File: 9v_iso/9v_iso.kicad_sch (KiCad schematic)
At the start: 15 parts, among them J1 Conn_01x02, J2 Conn_01x02, J3 Conn_01x03, U1 ICZ_SINGLE

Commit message: Checkpoint.
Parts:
- removed JP1: SolderJumper_3_Open, Jumper:SolderJumper-3_P1.3mm_Open_RoundedPad1.0x1.5mm_NumberLabels, symbol Jumper:SolderJumper_3_Open
- J3: value Conn_01x03 -> DNI
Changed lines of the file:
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@@
   (junction (at 59.69 73.66) (diameter 0) (color 0 0 0 0)
   )
-  (junction (at 99.06 49.53) (diameter 0) (color 0 0 0 0)
-  )
   (junction (at 99.06 64.77) (diameter 0) (color 0 0 0 0)
   )
-  (junction (at 93.98 46.99) (diameter 0) (color 0 0 0 0)
-  )
   (junction (at 50.8 90.17) (diameter 0) (color 0 0 0 0)
   )
@@
   (junction (at 59.69 90.17) (diameter 0) (color 0 0 0 0)
   )
-  (junction (at 88.9 44.45) (diameter 0) (color 0 0 0 0)
-  )
   (junction (at 78.74 90.17) (diameter 0) (color 0 0 0 0)
   )
@@
     (stroke (width 0) (type default) (color 0 0 0 0))
   )
-  (wire (pts (xy 88.9 39.37) (xy 88.9 44.45))
-    (stroke (width 0) (type default) (color 0 0 0 0))
-  )
   (wire (pts (xy 125.73 90.17) (xy 132.08 90.17))
     (stroke (width 0) (type default) (color 0 0 0 0))
@@
     (stroke (width 0) (type default) (color 0 0 0 0))
   )
-  (wire (pts (xy 93.98 43.18) (xy 93.98 46.99))
-    (stroke (width 0) (type default) (color 0 0 0 0))
-  )
   (wire (pts (xy 132.08 90.17) (xy 135.89 90.17))
     (stroke (width 0) (type default) (color 0 0 0 0))
@@
   )
   (wire (pts (xy 241.3 86.36) (xy 241.3 93.98))
-    (stroke (width 0) (type default) (color 0 0 0 0))
-  )
-  (wire (pts (xy 99.06 39.37) (xy 99.06 49.53))
     (stroke (width 0) (type default) (color 0 0 0 0))
   )
@@
       (effects (font (size 1.27 1.27)) (justify left))
     )
-    (property "Value" "Conn_01x03" (id 1) (at 111.76 48.2599 0)
+    (property "Value" "DNI" (id 1) (at 111.76 48.2599 0)
       (effects (font (size 1.27 1.27)) (justify left))
     )
@@
     (pin "2")
   )
-  (symbol (lib_id "Jumper:SolderJumper_3_Open") (at 93.98 39.37 0) (unit 1)
-    (in_bom yes) (on_board yes) (fields_autoplaced)
-    (property "Reference" "JP1" (id 0) (at 93.98 33.02 0))
-    (property "Value" "SolderJumper_3_Open" (id 1) (at 93.98 35.56 0))
-    (property "Footprint" "Jumper:SolderJumper-3_P1.3mm_Open_RoundedPad1.0x1.5mm_NumberLabels" (id 2) (at 93.98 39.37 0)
-      (effects (font (size 1.27 1.27)) hide)
-    )
-    (property "Datasheet" "~" (id 3) (at 93.98 39.37 0)
-      (effects (font (size 1.27 1.27)) hide)
-    )
-    (pin "1")
-    (pin "2")
-    (pin "3")
-  )
   (symbol (lib_id "power:GND") (at 88.9 46.99 0) (unit 1)
     (in_bom yes) (on_board yes) (fields_autoplaced)
@@
     )
     (path "/046a65e2-4a4e-47f4-924b-a6c9951d2ed3"
-      (reference "J3") (unit 1) (value "Conn_01x03") (footprint "Connector_PinHeader_2.54mm:PinHeader_1x03_P2.54mm_Vertical")
-    )
-    (path "/cbd2c5b4-c432-4ac8-b664-5d523c14cd16"
-      (reference "JP1") (unit 1) (value "SolderJumper_3_Open") (footprint "Jumper:SolderJumper-3_P1.3mm_Open_RoundedPad1.0x1.5mm_NumberLabels")
+      (reference "J3") (unit 1) (value "DNI") (footprint "Connector_PinHeader_2.54mm:PinHeader_1x03_P2.54mm_Vertical")
     )
     (path "/91a6582d-c885-450f-87a6-af7126326a3e"

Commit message: checkpoint
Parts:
- added R1: DNI/0, Resistor_SMD:R_0805_2012Metric_Pad1.20x1.40mm_HandSolder, symbol Device:R
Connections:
- net at J3.2 (Pin_2): now also R1.1; no longer U1.3 (ON/~{OFF})
- new net: R1.2, U1.3 (ON/~{OFF})
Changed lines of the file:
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@@
+    (stroke (width 0) (type default) (color 0 0 0 0))
+  )
+  (wire (pts (xy 93.98 46.99) (xy 93.98 54.61))
+    (stroke (width 0) (type default) (color 0 0 0 0))
+  )
+  (wire (pts (xy 93.98 62.23) (xy 93.98 85.09))
     (stroke (width 0) (type default) (color 0 0 0 0))
   )
@@
   )
   (wire (pts (xy 106.68 104.14) (xy 99.06 104.14))
-    (stroke (width 0) (type default) (color 0 0 0 0))
-  )
-  (wire (pts (xy 93.98 46.99) (xy 93.98 85.09))
     (stroke (width 0) (type default) (color 0 0 0 0))
   )
@@
     )
     (property "Datasheet" "~" (id 3) (at 59.69 82.55 0)
+      (effects (font (size 1.27 1.27)) hide)
+    )
+    (pin "1")
+    (pin "2")
+  )
+  (symbol (lib_id "Device:R") (at 93.98 58.42 0) (unit 1)
+    (in_bom yes) (on_board yes) (fields_autoplaced)
+    (property "Reference" "R1" (id 0) (at 96.52 57.1499 0)
+      (effects (font (size 1.27 1.27)) (justify left))
+    )
+    (property "Value" "DNI/0" (id 1) (at 96.52 59.6899 0)
+      (effects (font (size 1.27 1.27)) (justify left))
+    )
+    (property "Footprint" "Resistor_SMD:R_0805_2012Metric_Pad1.20x1.40mm_HandSolder" (id 2) (at 92.202 58.42 90)
+      (effects (font (size 1.27 1.27)) hide)
+    )
+    (property "Datasheet" "~" (id 3) (at 93.98 58.42 0)
       (effects (font (size 1.27 1.27)) hide)
     )
@@
       (reference "L1") (unit 1) (value "10u") (footprint "Inductor_SMD:L_Taiyo-Yuden_NR-24xx_HandSoldering")
     )
+    (path "/44b82516-223d-408b-8e30-cc8a52478507"
+      (reference "R1") (unit 1) (value "DNI/0") (footprint "Resistor_SMD:R_0805_2012Metric_Pad1.20x1.40mm_HandSolder")
+    )
     (path "/7ef59bd1-2177-4689-939e-d2f1f419fa14"

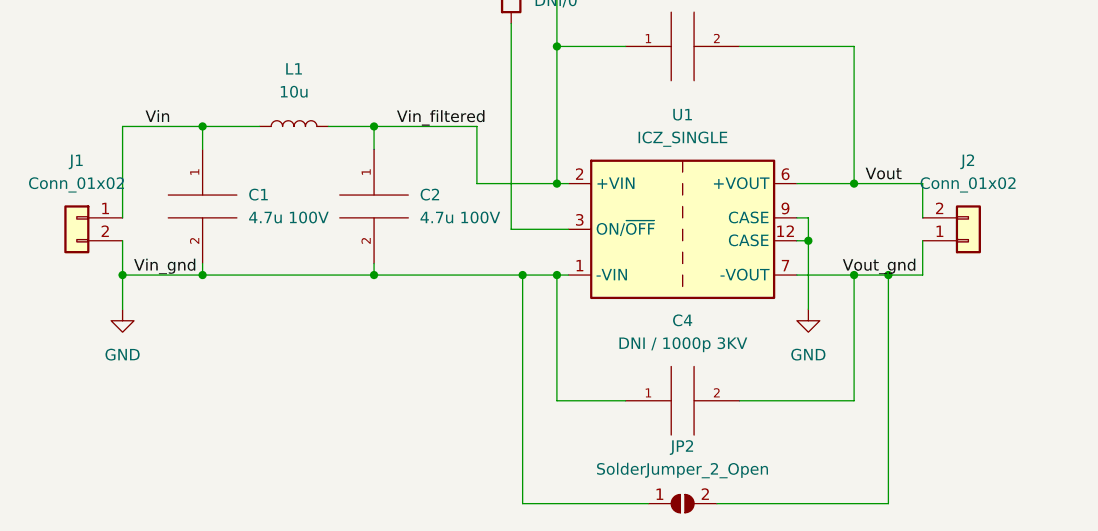
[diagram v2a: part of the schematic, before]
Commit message: v1.1 - fixes inductor footprint, fixes flipped J1, adds in/out and polarity labels, improves routing.
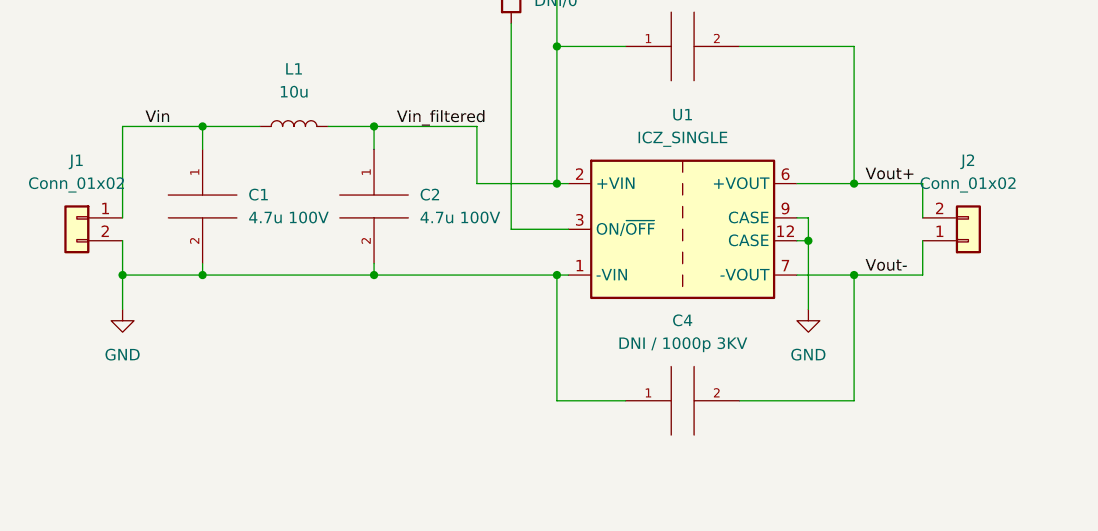
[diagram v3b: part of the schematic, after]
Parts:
- removed JP2: SolderJumper_2_Open, Jumper:SolderJumper-2_P1.3mm_Open_RoundedPad1.0x1.5mm, symbol Jumper:SolderJumper_2_Open
- L1: footprint Inductor_SMD:L_Taiyo-Yuden_NR-24xx_HandSoldering -> Inductor_SMD:L_Taiyo-Yuden_NR-60xx_HandSoldering
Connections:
- net Vout renamed Vout+
- net Vout_gnd renamed Vout-
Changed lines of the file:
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@@
   (junction (at 241.3 78.74) (diameter 0) (color 0 0 0 0)
   )
-  (junction (at 95.25 90.17) (diameter 0) (color 0 0 0 0)
-  )
-  (junction (at 135.89 90.17) (diameter 0) (color 0 0 0 0)
+  (junction (at 132.08 80.01) (diameter 0) (color 0 0 0 0)
   )
   (junction (at 132.08 90.17) (diameter 0) (color 0 0 0 0)
@@
   (junction (at 241.3 93.98) (diameter 0) (color 0 0 0 0)
   )
-  (junction (at 132.08 80.01) (diameter 0) (color 0 0 0 0)
-  )
   (junction (at 59.69 90.17) (diameter 0) (color 0 0 0 0)
   )
@@
     (stroke (width 0) (type default) (color 0 0 0 0))
   )
-  (wire (pts (xy 78.74 90.17) (xy 95.25 90.17))
-    (stroke (width 0) (type default) (color 0 0 0 0))
-  )
   (wire (pts (xy 132.08 104.14) (xy 132.08 90.17))
     (stroke (width 0) (type default) (color 0 0 0 0))
@@
     (stroke (width 0) (type default) (color 0 0 0 0))
   )
-  (wire (pts (xy 135.89 90.17) (xy 139.7 90.17))
+  (wire (pts (xy 132.08 64.77) (xy 132.08 80.01))
+    (stroke (width 0) (type default) (color 0 0 0 0))
+  )
+  (wire (pts (xy 132.08 90.17) (xy 139.7 90.17))
     (stroke (width 0) (type default) (color 0 0 0 0))
   )
@@
     (stroke (width 0) (type default) (color 0 0 0 0))
   )
-  (wire (pts (xy 139.7 80.01) (xy 132.08 80.01))
-    (stroke (width 0) (type default) (color 0 0 0 0))
-  )
-  (wire (pts (xy 132.08 80.01) (xy 125.73 80.01))
+  (wire (pts (xy 119.38 64.77) (xy 132.08 64.77))
     (stroke (width 0) (type default) (color 0 0 0 0))
   )
@@
     (stroke (width 0) (type default) (color 0 0 0 0))
   )
+  (wire (pts (xy 125.73 80.01) (xy 132.08 80.01))
+    (stroke (width 0) (type default) (color 0 0 0 0))
+  )
   (wire (pts (xy 93.98 46.99) (xy 93.98 54.61))
     (stroke (width 0) (type default) (color 0 0 0 0))
@@
     (stroke (width 0) (type default) (color 0 0 0 0))
   )
-  (wire (pts (xy 95.25 90.17) (xy 99.06 90.17))
+  (wire (pts (xy 78.74 90.17) (xy 99.06 90.17))
     (stroke (width 0) (type default) (color 0 0 0 0))
   )
@@
     (stroke (width 0) (type default) (color 0 0 0 0))
   )
-  (wire (pts (xy 95.25 115.57) (xy 95.25 90.17))
-    (stroke (width 0) (type default) (color 0 0 0 0))
-  )
   (wire (pts (xy 241.3 71.12) (xy 241.3 78.74))
     (stroke (width 0) (type default) (color 0 0 0 0))
@@
     (stroke (width 0) (type default) (color 0 0 0 0))
   )
+  (wire (pts (xy 125.73 86.36) (xy 127 86.36))
+    (stroke (width 0) (type default) (color 0 0 0 0))
+  )
+  (wire (pts (xy 106.68 104.14) (xy 99.06 104.14))
+    (stroke (width 0) (type default) (color 0 0 0 0))
+  )
+  (wire (pts (xy 99.06 49.53) (xy 99.06 64.77))
+    (stroke (width 0) (type default) (color 0 0 0 0))
+  )
+  (wire (pts (xy 237.49 86.36) (xy 241.3 86.36))
+    (stroke (width 0) (type default) (color 0 0 0 0))
+  )
+  (wire (pts (xy 127 93.98) (xy 127 86.36))
+    (stroke (width 0) (type default) (color 0 0 0 0))
+  )
+  (wire (pts (xy 241.3 78.74) (xy 241.3 86.36))
+    (stroke (width 0) (type default) (color 0 0 0 0))
+  )
+  (wire (pts (xy 132.08 80.01) (xy 139.7 80.01))
+    (stroke (width 0) (type default) (color 0 0 0 0))
+  )
+  (wire (pts (xy 78.74 90.17) (xy 59.69 90.17))
+    (stroke (width 0) (type default) (color 0 0 0 0))
+  )
+  (wire (pts (xy 78.74 73.66) (xy 78.74 76.2))
+    (stroke (width 0) (type default) (color 0 0 0 0))
+  )
+  (wire (pts (xy 78.74 73.66) (xy 90.17 73.66))
+    (stroke (width 0) (type default) (color 0 0 0 0))
+  )
+  (wire (pts (xy 127 86.36) (xy 127 83.82))
+    (stroke (width 0) (type default) (color 0 0 0 0))
+  )
+  (wire (pts (xy 88.9 44.45) (xy 88.9 46.99))
+    (stroke (width 0) (type default) (color 0 0 0 0))
+  )
+  (wire (pts (xy 99.06 80.01) (xy 100.33 80.01))
+    (stroke (width 0) (type default) (color 0 0 0 0))
+  )
   (wire (pts (xy 139.7 80.01) (xy 139.7 83.82))
     (stroke (width 0) (type default) (color 0 0 0 0))
   )
-  (wire (pts (xy 125.73 86.36) (xy 127 86.36))
-    (stroke (width 0) (type default) (color 0 0 0 0))
-  )
-  (wire (pts (xy 106.68 104.14) (xy 99.06 104.14))
-    (stroke (width 0) (type default) (color 0 0 0 0))
-  )
-  (wire (pts (xy 99.06 49.53) (xy 99.06 64.77))
-    (stroke (width 0) (type default) (color 0 0 0 0))
-  )
-  (wire (pts (xy 237.49 86.36) (xy 241.3 86.36))
-    (stroke (width 0) (type default) (color 0 0 0 0))
-  )
-  (wire (pts (xy 127 93.98) (xy 127 86.36))
-    (stroke (width 0) (type default) (color 0 0 0 0))
-  )
-  (wire (pts (xy 241.3 78.74) (xy 241.3 86.36))
-    (stroke (width 0) (type default) (color 0 0 0 0))
-  )
-  (wire (pts (xy 78.74 90.17) (xy 59.69 90.17))
-    (stroke (width 0) (type default) (color 0 0 0 0))
-  )
-  (wire (pts (xy 78.74 73.66) (xy 78.74 76.2))
-    (stroke (width 0) (type default) (color 0 0 0 0))
-  )
-  (wire (pts (xy 78.74 73.66) (xy 90.17 73.66))
-    (stroke (width 0) (type default) (color 0 0 0 0))
-  )
-  (wire (pts (xy 127 86.36) (xy 127 83.82))
-    (stroke (width 0) (type default) (color 0 0 0 0))
-  )
-  (wire (pts (xy 109.22 115.57) (xy 95.25 115.57))
-    (stroke (width 0) (type default) (color 0 0 0 0))
-  )
-  (wire (pts (xy 88.9 44.45) (xy 88.9 46.99))
-    (stroke (width 0) (type default) (color 0 0 0 0))
-  )
-  (wire (pts (xy 135.89 115.57) (xy 135.89 90.17))
-    (stroke (width 0) (type default) (color 0 0 0 0))
-  )
-  (wire (pts (xy 99.06 80.01) (xy 100.33 80.01))
-    (stroke (width 0) (type default) (color 0 0 0 0))
-  )
-  (wire (pts (xy 119.38 64.77) (xy 132.08 64.77))
-    (stroke (width 0) (type default) (color 0 0 0 0))
-  )
-  (wire (pts (xy 116.84 115.57) (xy 135.89 115.57))
-    (stroke (width 0) (type default) (color 0 0 0 0))
-  )
   (wire (pts (xy 127 83.82) (xy 125.73 83.82))
     (stroke (width 0) (type default) (color 0 0 0 0))
@@
     (stroke (width 0) (type default) (color 0 0 0 0))
   )
-  (wire (pts (xy 132.08 90.17) (xy 135.89 90.17))
-    (stroke (width 0) (type default) (color 0 0 0 0))
-  )
   (wire (pts (xy 237.49 78.74) (xy 241.3 78.74))
     (stroke (width 0) (type default) (color 0 0 0 0))
@@
   )
   (wire (pts (xy 88.9 44.45) (xy 104.14 44.45))
-    (stroke (width 0) (type default) (color 0 0 0 0))
-  )
-  (wire (pts (xy 132.08 64.77) (xy 132.08 80.01))
     (stroke (width 0) (type default) (color 0 0 0 0))
   )
@@
     (effects (font (size 1.27 1.27)) (justify left bottom))
   )
-  (label "Vout_gnd" (at 130.81 90.17 0)
+  (label "Vout+" (at 133.35 80.01 0)
     (effects (font (size 1.27 1.27)) (justify left bottom))
   )
-  (label "Vin_gnd" (at 52.07 90.17 0)
-    (effects (font (size 1.27 1.27)) (justify left bottom))
-  )
-  (label "Vout" (at 133.35 80.01 0)
+  (label "Vout-" (at 133.35 90.17 0)
     (effects (font (size 1.27 1.27)) (justify left bottom))
   )
@@
     (pin "2")
   )
-  (symbol (lib_id "Jumper:SolderJumper_2_Open") (at 113.03 115.57 0) (unit 1)
-    (in_bom yes) (on_board yes) (fields_autoplaced)
-    (property "Reference" "JP2" (id 0) (at 113.03 109.22 0))
-    (property "Value" "SolderJumper_2_Open" (id 1) (at 113.03 111.76 0))
-    (property "Footprint" "Jumper:SolderJumper-2_P1.3mm_Open_RoundedPad1.0x1.5mm" (id 2) (at 113.03 115.57 0)
-      (effects (font (size 1.27 1.27)) hide)
-    )
-    (property "Datasheet" "~" (id 3) (at 113.03 115.57 0)
-      (effects (font (size 1.27 1.27)) hide)
-    )
-    (pin "1")
-    (pin "2")
-  )
   (symbol (lib_id "Mechanical:MountingHole_Pad") (at 237.49 68.58 0) (unit 1)
     (in_bom yes) (on_board yes) (fields_autoplaced)
@@
     (property "Reference" "L1" (id 0) (at 69.85 67.31 90))
     (property "Value" "10u" (id 1) (at 69.85 69.85 90))
-    (property "Footprint" "Inductor_SMD:L_Taiyo-Yuden_NR-24xx_HandSoldering" (id 2) (at 69.85 73.66 0)
+    (property "Footprint" "Inductor_SMD:L_Taiyo-Yuden_NR-60xx_HandSoldering" (id 2) (at 69.85 73.66 0)
       (effects (font (size 1.27 1.27)) hide)
     )
@@
       (reference "J3") (unit 1) (value "DNI") (footprint "Connector_PinHeader_2.54mm:PinHeader_1x03_P2.54mm_Vertical")
     )
-    (path "/91a6582d-c885-450f-87a6-af7126326a3e"
-      (reference "JP2") (unit 1) (value "SolderJumper_2_Open") (footprint "Jumper:SolderJumper-2_P1.3mm_Open_RoundedPad1.0x1.5mm")
-    )
     (path "/c61922f7-b03a-427e-9077-287f9265f85b"
-      (reference "L1") (unit 1) (value "10u") (footprint "Inductor_SMD:L_Taiyo-Yuden_NR-24xx_HandSoldering")
+      (reference "L1") (unit 1) (value "10u") (footprint "Inductor_SMD:L_Taiyo-Yuden_NR-60xx_HandSoldering")
     )
     (path "/44b82516-223d-408b-8e30-cc8a52478507"
